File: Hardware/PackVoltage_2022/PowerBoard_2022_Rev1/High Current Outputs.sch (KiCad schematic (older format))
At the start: 20 parts, among them Q12 BUK7M8R5-40HX, Q13 BUK7M8R5-40HX, U44 LT1910, U45 INA281, U46 LT1910, U47 INA281

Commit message: Replaced 12v okis w/big buck. Changed .0025 resistors to not 603.
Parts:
- R50, R53: footprint Resistor_SMD:R_0603_1608Metric_Pad1.05x0.95mm_HandSolder -> Resistor_SMD:R_1206_3216Metric_Pad1.30x1.75mm_HandSolder
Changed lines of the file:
@@
 EESchema Schematic File Version 4
-LIBS:PowerBoard_2022_Rev1-cache
-EELAYER 26 0
+EELAYER 30 0
 EELAYER END
 $Descr A4 11693 8268
@@
 F 0 "R50" H 3820 2096 50  0000 L CNN
 F 1 "0.0025" V 3750 1950 50  0000 L CNN
-F 2 "Resistor_SMD:R_0603_1608Metric_Pad1.05x0.95mm_HandSolder" V 3680 2050 50  0001 C CNN
+F 2 "Resistor_SMD:R_1206_3216Metric_Pad1.30x1.75mm_HandSolder" V 3680 2050 50  0001 C CNN
 F 3 "~" H 3750 2050 50  0001 C CNN
 	1    3750 2050
@@
 F 0 "R53" H 8770 2246 50  0000 L CNN
 F 1 "0.0025" V 8700 2100 50  0000 L CNN
-F 2 "Resistor_SMD:R_0603_1608Metric_Pad1.05x0.95mm_HandSolder" V 8630 2200 50  0001 C CNN
+F 2 "Resistor_SMD:R_1206_3216Metric_Pad1.30x1.75mm_HandSolder" V 8630 2200 50  0001 C CNN
 F 3 "~" H 8700 2200 50  0001 C CNN
 	1    8700 2200

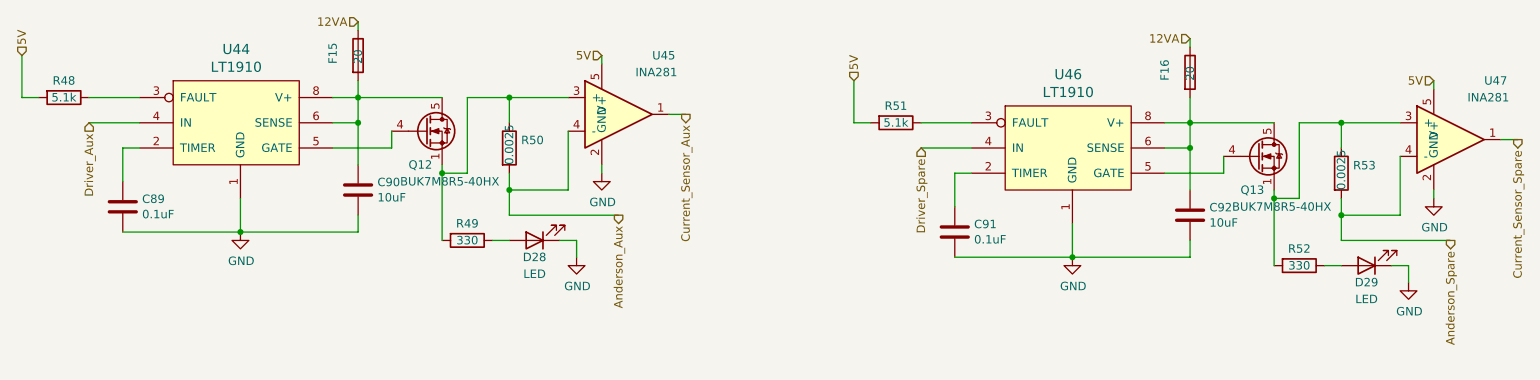
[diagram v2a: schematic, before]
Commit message: changed MOSFET names to what we're actually using
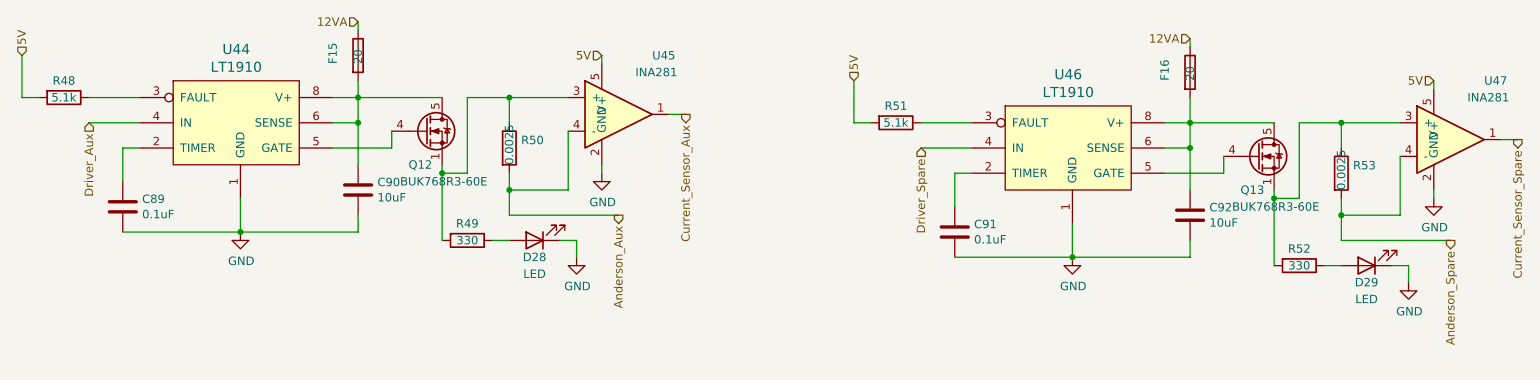
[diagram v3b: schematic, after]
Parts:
- Q12, Q13: value BUK7M8R5-40HX -> BUK768R3-60E
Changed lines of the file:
@@
 $Descr A4 11693 8268
 encoding utf-8
-Sheet 9 9
+Sheet 7 9
 Title ""
 Date ""
@@
 AR Path="/615D7BA0/6170B6A9/6190350A" Ref="Q12"  Part="1"
 F 0 "Q12" H 3150 1750 50  0000 L CNN
-F 1 "BUK7M8R5-40HX" H 3100 1650 50  0000 L CNN
+F 1 "BUK768R3-60E" H 3100 1650 50  0000 L CNN
 F 2 "Package_TO_SOT_SMD:LFPAK33" H 3450 1875 50  0001 L CIN
 F 3 "https://assets.nexperia.com/documents/data-sheet/BUK7M8R0-40E.pdf" V 3250 1950 50  0001 L CNN
@@
 AR Path="/615D7BA0/6170B6A9/6191E118" Ref="Q13"  Part="1"
 F 0 "Q13" H 8100 1900 50  0000 L CNN
-F 1 "BUK7M8R5-40HX" H 8050 1800 50  0000 L CNN
+F 1 "BUK768R3-60E" H 8050 1800 50  0000 L CNN
 F 2 "Package_TO_SOT_SMD:LFPAK33" H 8400 2025 50  0001 L CIN
 F 3 "https://assets.nexperia.com/documents/data-sheet/BUK7M8R0-40E.pdf" V 8200 2100 50  0001 L CNN

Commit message: Closing kicad + bom stuff
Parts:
- R50, R53: footprint Resistor_SMD:R_1206_3216Metric_Pad1.30x1.75mm_HandSolder -> Resistor_SMD:R_0402_1005Metric_Pad0.72x0.64mm_HandSolder
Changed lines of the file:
@@
 F 0 "R50" H 3820 2096 50  0000 L CNN
 F 1 "0.0025" V 3750 1950 50  0000 L CNN
-F 2 "Resistor_SMD:R_1206_3216Metric_Pad1.30x1.75mm_HandSolder" V 3680 2050 50  0001 C CNN
+F 2 "Resistor_SMD:R_0402_1005Metric_Pad0.72x0.64mm_HandSolder" V 3680 2050 50  0001 C CNN
 F 3 "~" H 3750 2050 50  0001 C CNN
 	1    3750 2050
@@
 F 0 "R53" H 8770 2246 50  0000 L CNN
 F 1 "0.0025" V 8700 2100 50  0000 L CNN
-F 2 "Resistor_SMD:R_1206_3216Metric_Pad1.30x1.75mm_HandSolder" V 8630 2200 50  0001 C CNN
+F 2 "Resistor_SMD:R_0402_1005Metric_Pad0.72x0.64mm_HandSolder" V 8630 2200 50  0001 C CNN
 F 3 "~" H 8700 2200 50  0001 C CNN
 	1    8700 2200

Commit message: Changed the footprint for the shunt resistors and loaded the netlist to the layout
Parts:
- R50, R53: footprint Resistor_SMD:R_0402_1005Metric_Pad0.72x0.64mm_HandSolder -> Resistor_SMD:R_2512_6332Metric_Pad1.40x3.35mm_HandSolder
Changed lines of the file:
@@
 F 0 "R50" H 3820 2096 50  0000 L CNN
 F 1 "0.0025" V 3750 1950 50  0000 L CNN
-F 2 "Resistor_SMD:R_0402_1005Metric_Pad0.72x0.64mm_HandSolder" V 3680 2050 50  0001 C CNN
+F 2 "Resistor_SMD:R_2512_6332Metric_Pad1.40x3.35mm_HandSolder" V 3680 2050 50  0001 C CNN
 F 3 "~" H 3750 2050 50  0001 C CNN
 	1    3750 2050
@@
 F 0 "R53" H 8770 2246 50  0000 L CNN
 F 1 "0.0025" V 8700 2100 50  0000 L CNN
-F 2 "Resistor_SMD:R_0402_1005Metric_Pad0.72x0.64mm_HandSolder" V 8630 2200 50  0001 C CNN
+F 2 "Resistor_SMD:R_2512_6332Metric_Pad1.40x3.35mm_HandSolder" V 8630 2200 50  0001 C CNN
 F 3 "~" H 8700 2200 50  0001 C CNN
 	1    8700 2200
